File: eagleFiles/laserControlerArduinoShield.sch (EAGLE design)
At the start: 2 parts, among them T1 74990110013

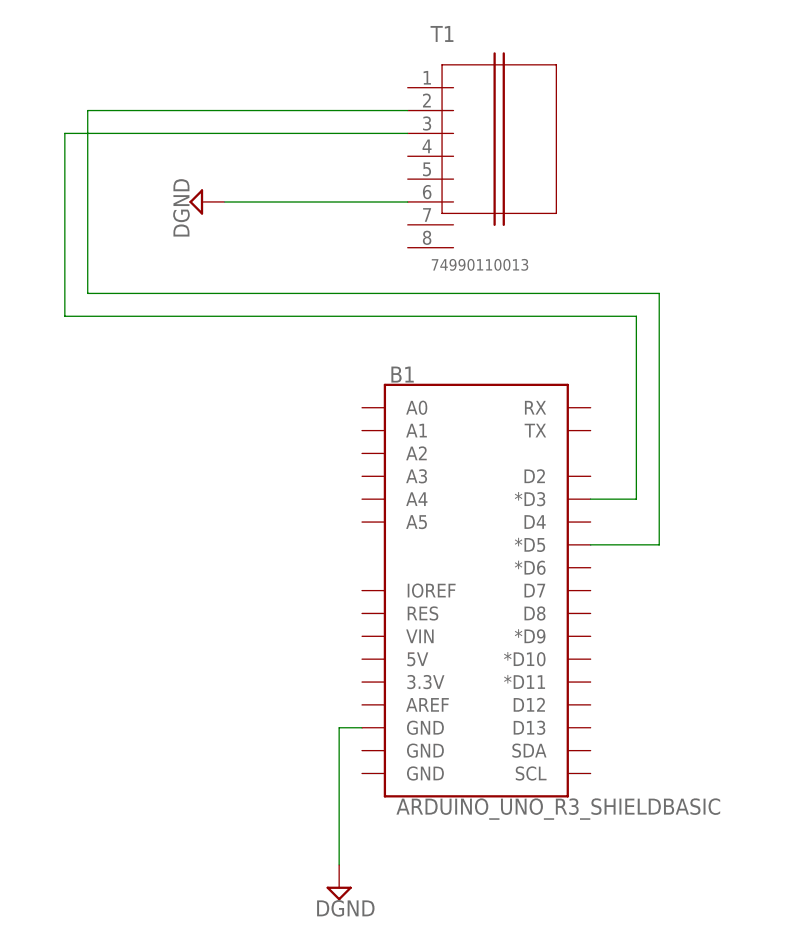
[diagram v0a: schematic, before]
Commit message: connect pins 4-5 in ethernet connector to turn the laser on
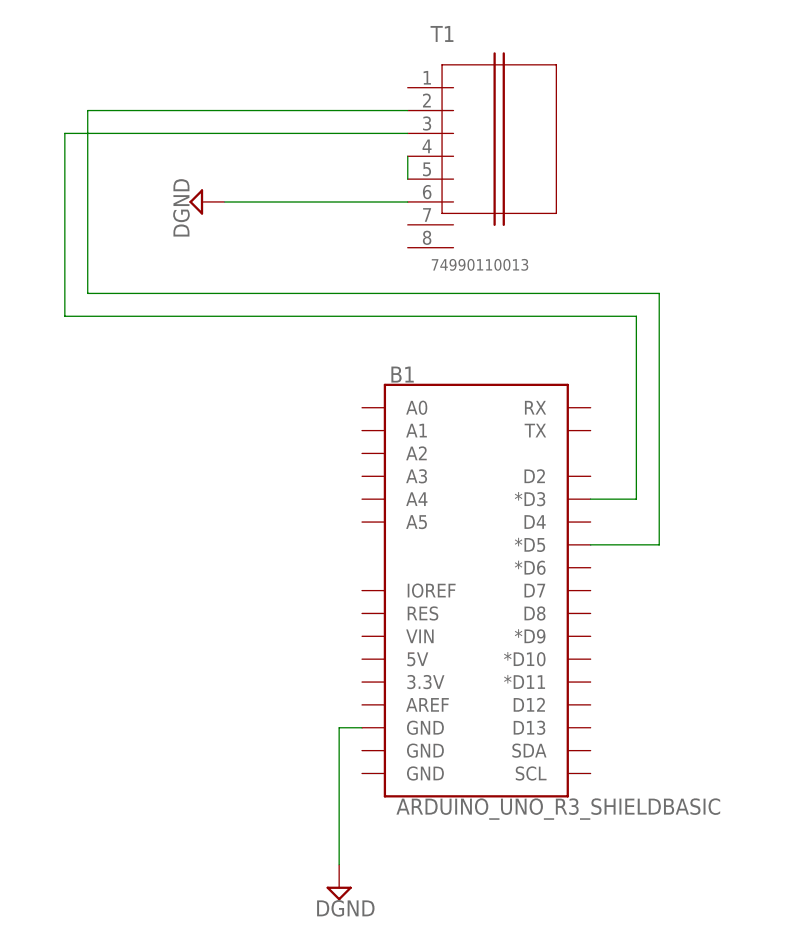
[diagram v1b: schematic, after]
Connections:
- new net N$3: T1.4, T1.5
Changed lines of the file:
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@@
+</segment>
+</net>
+<net name="N$3" class="0">
+<segment>
+<pinref part="T1" gate="G$1" pin="4"/>
+<pinref part="T1" gate="G$1" pin="5"/>
+<wire x1="-25.4" y1="66.04" x2="-25.4" y2="63.5" width="0.1524" layer="91"/>
 </segment>
 </net>

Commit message: add bnc connectors to arduino shield to sent ttl to recording system
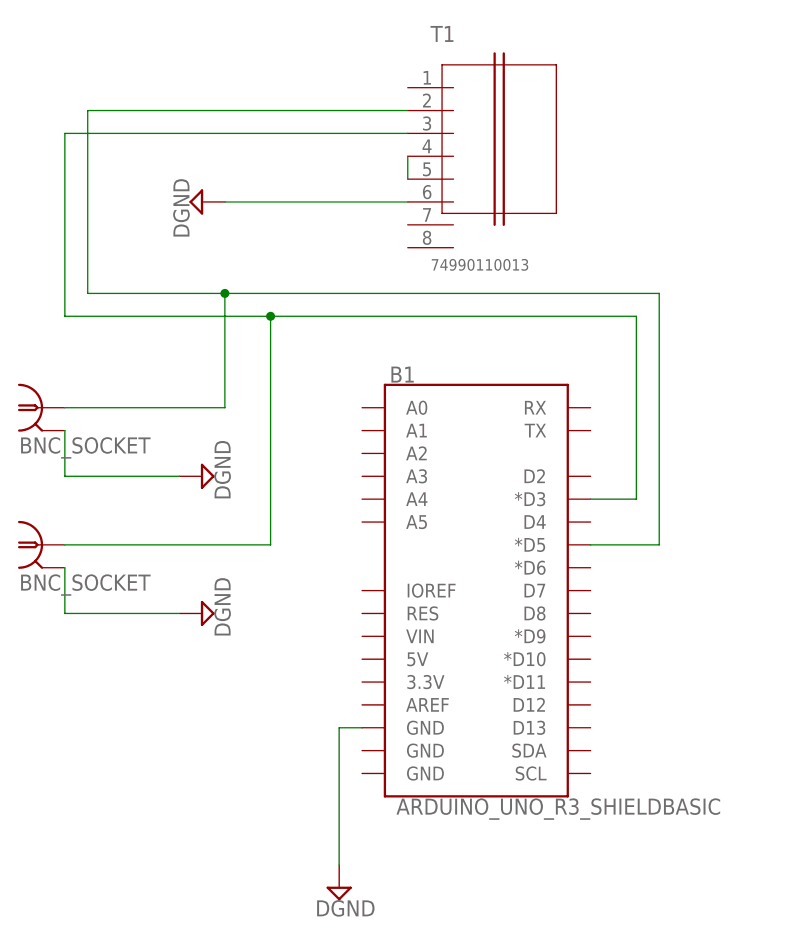
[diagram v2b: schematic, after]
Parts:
- added BNC_POWER, BNC_TTL: BNC_SOCKET, My_library:BNC_SOCKET
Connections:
- net DGND: now also BNC_POWER.2, BNC_TTL.2
- net N$1: now also BNC_TTL.1
- net N$2: now also BNC_POWER.1
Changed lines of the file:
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@@
 <part name="T1" library="wurth_electronics_midcom_inc_v1-0" deviceset="74990110013" device=""/>
 <part name="SUPPLY3" library="supply2" library_urn="urn:adsk.eagle:library:372" deviceset="DGND" device=""/>
+<part name="BNC_TTL" library="My_library" deviceset="BNC_SOCKET" device=""/>
+<part name="BNC_POWER" library="My_library" deviceset="BNC_SOCKET" device=""/>
+<part name="SUPPLY1" library="supply2" library_urn="urn:adsk.eagle:library:372" deviceset="DGND" device=""/>
+<part name="SUPPLY2" library="supply2" library_urn="urn:adsk.eagle:library:372" deviceset="DGND" device=""/>
 </parts>
 <sheets>
@@
 <attribute name="VALUE" x="-51.435" y="63.627" size="1.778" layer="96" rot="R270"/>
 </instance>
+<instance part="BNC_TTL" gate="G$1" x="-66.04" y="38.1" smashed="yes">
+<attribute name="VALUE" x="-68.58" y="33.02" size="1.778" layer="96"/>
+</instance>
+<instance part="BNC_POWER" gate="G$1" x="-66.04" y="22.86" smashed="yes">
+<attribute name="VALUE" x="-68.58" y="17.78" size="1.778" layer="96"/>
+</instance>
+<instance part="SUPPLY1" gate="G$1" x="-48.26" y="30.48" smashed="yes" rot="R90">
+<attribute name="VALUE" x="-45.085" y="27.813" size="1.778" layer="96" rot="R90"/>
+</instance>
+<instance part="SUPPLY2" gate="G$1" x="-48.26" y="15.24" smashed="yes" rot="R90">
+<attribute name="VALUE" x="-45.085" y="12.573" size="1.778" layer="96" rot="R90"/>
+</instance>
 </instances>
 <busses>
@@
 <wire x1="-45.72" y1="60.96" x2="-25.4" y2="60.96" width="0.1524" layer="91"/>
 </segment>
+<segment>
+<pinref part="BNC_TTL" gate="G$1" pin="2"/>
+<pinref part="SUPPLY1" gate="G$1" pin="DGND"/>
+<wire x1="-63.5" y1="35.56" x2="-63.5" y2="30.48" width="0.1524" layer="91"/>
+<wire x1="-63.5" y1="30.48" x2="-50.8" y2="30.48" width="0.1524" layer="91"/>
+</segment>
+<segment>
+<pinref part="BNC_POWER" gate="G$1" pin="2"/>
+<pinref part="SUPPLY2" gate="G$1" pin="DGND"/>
+<wire x1="-63.5" y1="20.32" x2="-63.5" y2="15.24" width="0.1524" layer="91"/>
+<wire x1="-63.5" y1="15.24" x2="-50.8" y2="15.24" width="0.1524" layer="91"/>
+</segment>
 </net>
 <net name="N$1" class="0">
@@
 <wire x1="-5.08" y1="22.86" x2="2.54" y2="22.86" width="0.1524" layer="91"/>
 <wire x1="2.54" y1="22.86" x2="2.54" y2="50.8" width="0.1524" layer="91"/>
-<wire x1="2.54" y1="50.8" x2="-60.96" y2="50.8" width="0.1524" layer="91"/>
+<wire x1="2.54" y1="50.8" x2="-45.72" y2="50.8" width="0.1524" layer="91"/>
+<wire x1="-45.72" y1="50.8" x2="-60.96" y2="50.8" width="0.1524" layer="91"/>
 <wire x1="-60.96" y1="50.8" x2="-60.96" y2="71.12" width="0.1524" layer="91"/>
 <pinref part="T1" gate="G$1" pin="2"/>
 <wire x1="-60.96" y1="71.12" x2="-25.4" y2="71.12" width="0.1524" layer="91"/>
+<wire x1="-45.72" y1="50.8" x2="-45.72" y2="38.1" width="0.1524" layer="91"/>
+<junction x="-45.72" y="50.8"/>
+<pinref part="BNC_TTL" gate="G$1" pin="1"/>
+<wire x1="-45.72" y1="38.1" x2="-63.5" y2="38.1" width="0.1524" layer="91"/>
 </segment>
 </net>
@@
 <wire x1="-5.08" y1="27.94" x2="0" y2="27.94" width="0.1524" layer="91"/>
 <wire x1="0" y1="27.94" x2="0" y2="48.26" width="0.1524" layer="91"/>
-<wire x1="0" y1="48.26" x2="-63.5" y2="48.26" width="0.1524" layer="91"/>
+<wire x1="0" y1="48.26" x2="-40.64" y2="48.26" width="0.1524" layer="91"/>
+<wire x1="-40.64" y1="48.26" x2="-63.5" y2="48.26" width="0.1524" layer="91"/>
 <wire x1="-63.5" y1="48.26" x2="-63.5" y2="68.58" width="0.1524" layer="91"/>
 <pinref part="T1" gate="G$1" pin="3"/>
 <wire x1="-63.5" y1="68.58" x2="-25.4" y2="68.58" width="0.1524" layer="91"/>
+<pinref part="BNC_POWER" gate="G$1" pin="1"/>
+<wire x1="-40.64" y1="48.26" x2="-40.64" y2="22.86" width="0.1524" layer="91"/>
+<wire x1="-40.64" y1="22.86" x2="-63.5" y2="22.86" width="0.1524" layer="91"/>
+<junction x="-40.64" y="48.26"/>
 </segment>
 </net>
